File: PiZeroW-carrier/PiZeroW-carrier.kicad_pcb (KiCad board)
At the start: 2 copper layers, 65 x 30 mm, 35 parts, among them CON1 BARREL_JACK, J1 PI40HAT, P1 USB_OTG, SW1 SW_PUSH, U1 BA50BC0WFP-E2CT, U2 BA06CC0WFP-E2CT

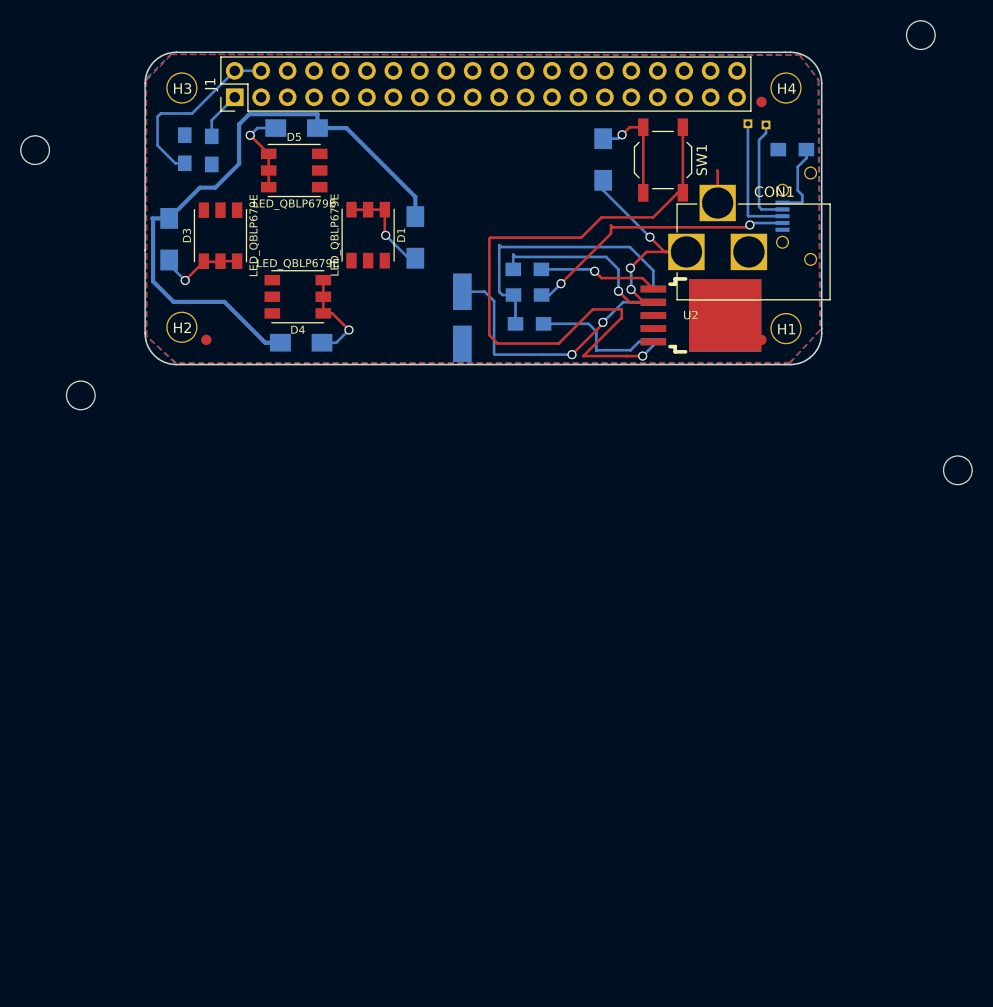
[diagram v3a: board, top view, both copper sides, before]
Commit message: cleanup some routes that the autorouter must have created
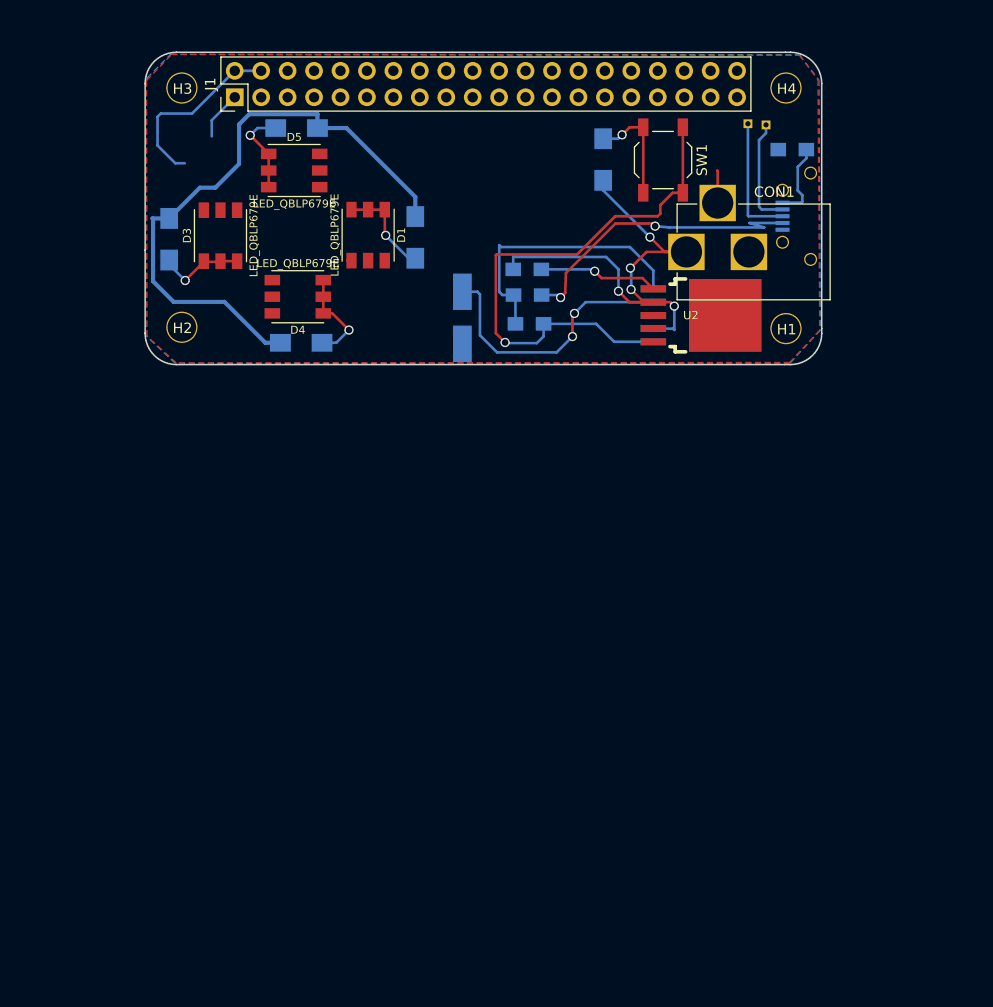
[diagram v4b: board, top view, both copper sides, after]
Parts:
- removed 1PIN (x4): P***, 1pin
- removed FID1, FID2, FID3: FIDUCIAL, DiscoCap:FIDUCIAL
- removed R10, R9: DNP, Resistors_SMD:R_0805_HandSoldering
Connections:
- net Net-(R2-Pad1) renamed /Power/PiDisable
- D6 pad 1: /Power/+5V -> (no net)
- J1 pad 1: /raspberrypi-gpio-40pin/P3V3_HAT -> (no net)
- J1 pad 10: Net-(J1-Pad10) -> (no net)
- J1 pad 11: /raspberrypi-gpio-40pin/LEDEnable -> (no net)
- J1 pad 12: Net-(J1-Pad12) -> (no net)
- J1 pad 13: /raspberrypi-gpio-40pin/PiDisable -> (no net)
- J1 pad 15: Net-(J1-Pad15) -> (no net)
- J1 pad 16: Net-(J1-Pad16) -> (no net)
- J1 pad 17: Net-(J1-Pad17) -> (no net)
- J1 pad 18: Net-(J1-Pad18) -> (no net)
- J1 pad 19: Net-(J1-Pad19) -> (no net)
- J1 pad 21: Net-(J1-Pad21) -> (no net)
- J1 pad 22: Net-(J1-Pad22) -> (no net)
- J1 pad 23: Net-(J1-Pad23) -> (no net)
- J1 pad 24: Net-(J1-Pad24) -> (no net)
- J1 pad 26: Net-(J1-Pad26) -> (no net)
- J1 pad 27: /raspberrypi-gpio-40pin/SDA -> (no net)
- J1 pad 28: /raspberrypi-gpio-40pin/SCL -> (no net)
- J1 pad 29: Net-(J1-Pad29) -> (no net)
- J1 pad 3: Net-(J1-Pad3) -> (no net)
- J1 pad 31: Net-(J1-Pad31) -> (no net)
- J1 pad 32: Net-(J1-Pad32) -> (no net)
- J1 pad 33: Net-(J1-Pad33) -> (no net)
- J1 pad 35: Net-(J1-Pad35) -> (no net)
- J1 pad 36: Net-(J1-Pad36) -> (no net)
- J1 pad 37: Net-(J1-Pad37) -> (no net)
- J1 pad 38: Net-(J1-Pad38) -> (no net)
- J1 pad 40: Net-(J1-Pad40) -> (no net)
- J1 pad 5: Net-(J1-Pad5) -> (no net)
- J1 pad 7: Net-(J1-Pad7) -> (no net)
- J1 pad 8: Net-(J1-Pad8) -> (no net)
- R12 pad 1: +5V -> (no net)
- U2 pad 4: /Power/+6V -> (no net)
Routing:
- net /Power/PiDisable: track 77.0 -> 52.9 mm
- net +BATT: track 40.2 -> 46.7 mm, vias 4 -> 5
- net (no net): track 0.00 -> 5.18 mm
- net /raspberrypi-gpio-40pin/P3V3_HAT: track 4.67 -> 0.00 mm
- net Net-(P1-Pad4): track 26.6 -> 30.2 mm

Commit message: fix PiDisable/LEDEnable.  Need to connect them on the root sheet. Extra-duh
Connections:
- D1 pad 1: /Leds/GND -> GND
- D1 pad 2: /Leds/GND -> GND
- D1 pad 3: /Leds/GND -> GND
- D3 pad 1: /Leds/GND -> GND
- D3 pad 2: /Leds/GND -> GND
- D3 pad 3: /Leds/GND -> GND
- D4 pad 1: /Leds/GND -> GND
- D4 pad 2: /Leds/GND -> GND
- D4 pad 3: /Leds/GND -> GND
- D5 pad 1: /Leds/GND -> GND
- D5 pad 2: /Leds/GND -> GND
- D5 pad 3: /Leds/GND -> GND
- J1 pad 11: (no net) -> /Power/LEDEnable
- J1 pad 13: (no net) -> /Power/PiDisable

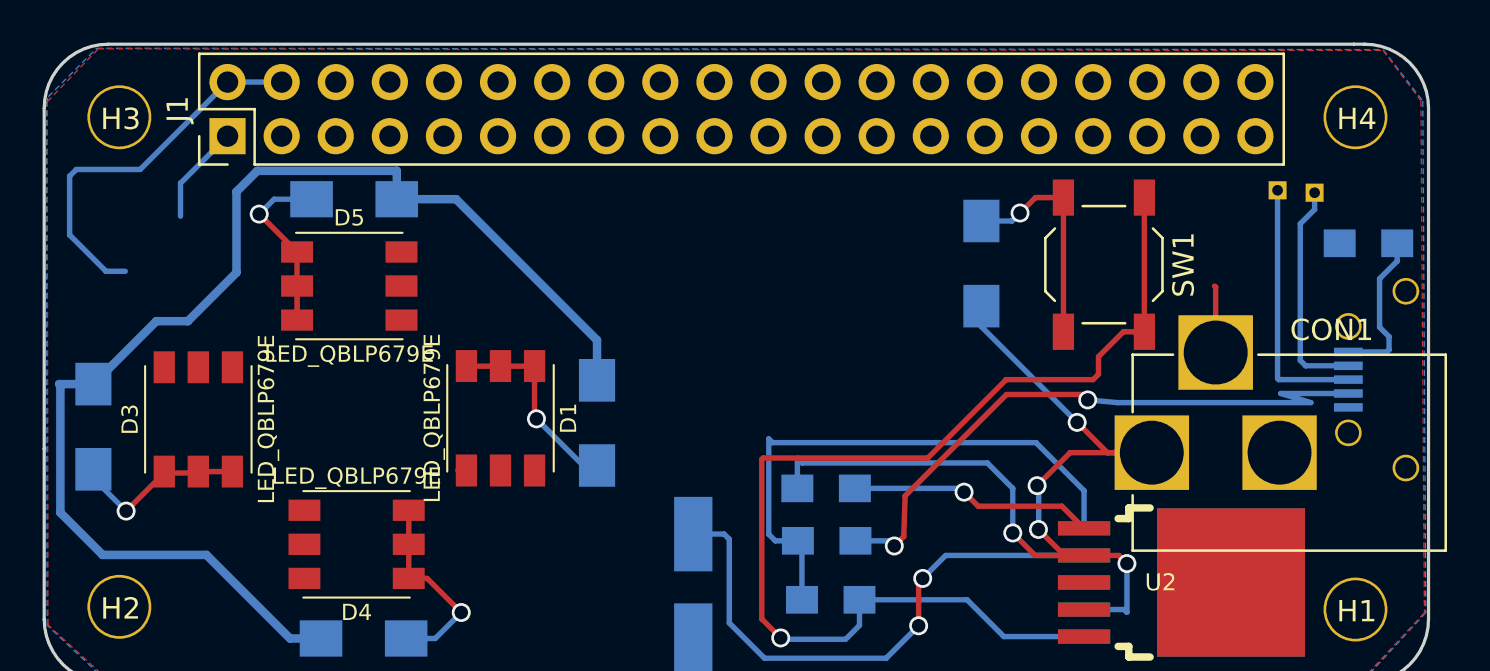
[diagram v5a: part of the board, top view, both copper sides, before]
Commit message: route LEDEnable and PiDisable. fix 40pin Gnds
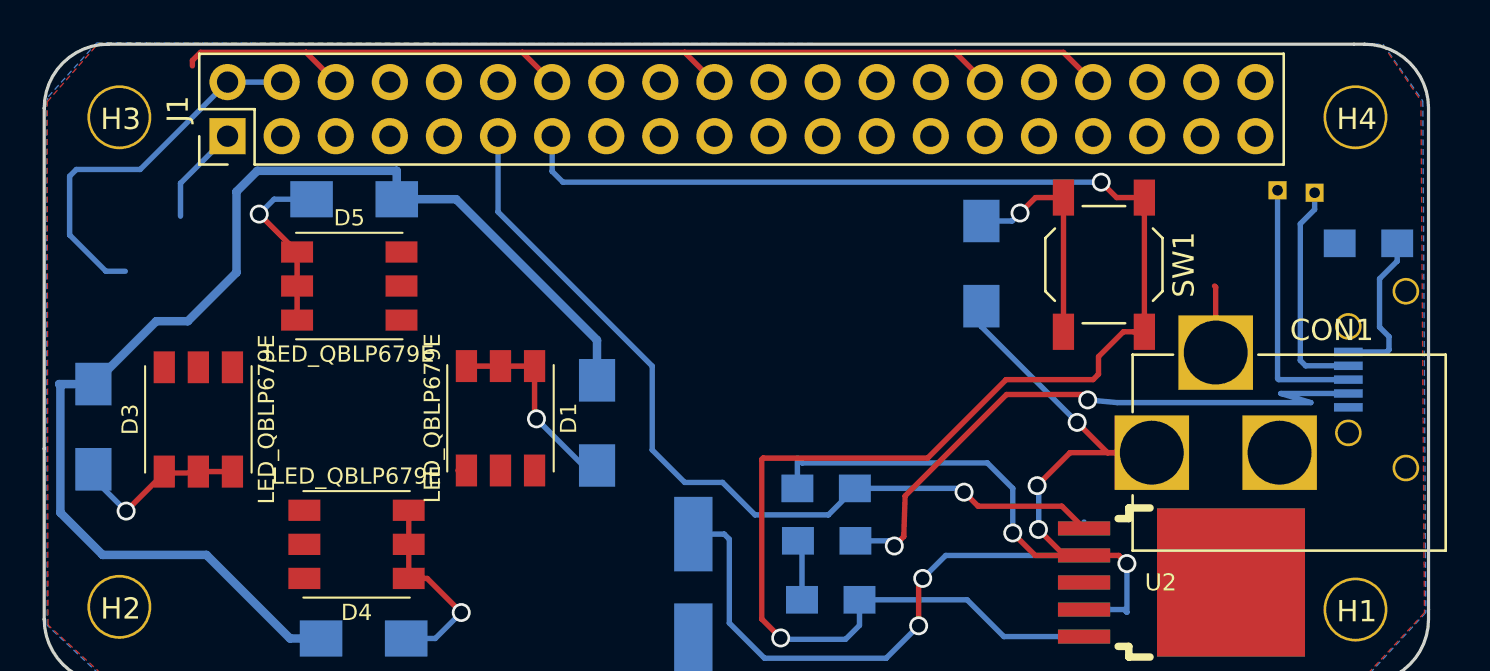
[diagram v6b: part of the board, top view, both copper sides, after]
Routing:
- net /Power/PiDisable: track 52.9 -> 82.9 mm, vias 1 -> 2
- net /Power/LEDEnable: track 11.5 -> 40.6 mm
- net GND: track 30.3 -> 57.9 mm
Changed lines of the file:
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@@
   (general
     (links 65)
-    (no_connects 20)
+    (no_connects 2)
     (area 109.424999 79.424999 174.575001 109.575001)
     (thickness 1.6)
     (drawings 12)
-    (tracks 172)
+    (tracks 191)
     (zones 0)
     (modules 26)
@@
   (segment (start 143.31188 81.71942) (end 143.31188 81.97342) (width 0.254) (layer F.Cu) (net 0))
   (segment (start 148.39188 81.71942) (end 148.39188 81.84642) (width 0.254) (layer B.Cu) (net 0))
+  (segment (start 152.273 79.883) (end 157.353 79.883) (width 0.254) (layer F.Cu) (net 1))
+  (segment (start 157.353 79.883) (end 158.75 81.28) (width 0.254) (layer F.Cu) (net 1) (status 800000))
+  (segment (start 139.573 79.883) (end 152.273 79.883) (width 0.254) (layer F.Cu) (net 1))
+  (segment (start 152.273 79.883) (end 153.67 81.28) (width 0.254) (layer F.Cu) (net 1) (status 800000))
+  (segment (start 131.953 79.883) (end 139.573 79.883) (width 0.254) (layer F.Cu) (net 1))
+  (segment (start 139.573 79.883) (end 140.97 81.28) (width 0.254) (layer F.Cu) (net 1) (status 800000))
+  (segment (start 121.793 79.883) (end 131.953 79.883) (width 0.254) (layer F.Cu) (net 1))
+  (segment (start 131.953 79.883) (end 133.35 81.28) (width 0.254) (layer F.Cu) (net 1) (status 800000))
+  (segment (start 116.459 80.518) (end 116.459 80.264) (width 0.254) (layer F.Cu) (net 1))
+  (segment (start 121.793 79.883) (end 123.19 81.28) (width 0.254) (layer F.Cu) (net 1) (status 800000))
+  (segment (start 116.84 79.883) (end 121.793 79.883) (width 0.254) (layer F.Cu) (net 1))
+  (segment (start 116.459 80.264) (end 116.84 79.883) (width 0.254) (layer F.Cu) (net 1))
   (segment (start 164.5059 93.979) (end 164.5059 90.9094) (width 0.254) (layer F.Cu) (net 1))
   (segment (start 164.5059 90.9094) (end 164.4523 90.8558) (width 0.254) (layer F.Cu) (net 1))
   (segment (start 158.325 102.235) (end 158.325 101.9361) (width 0.254) (layer B.Cu) (net 1))
-  (segment (start 144.8905 102.8192) (end 143.8275 102.8192) (width 0.254) (layer B.Cu) (net 1))
-  (segment (start 158.325 100.4638) (end 158.325 102.235) (width 0.254) (layer B.Cu) (net 1))
-  (segment (start 156.0703 98.2091) (end 158.325 100.4638) (width 0.254) (layer B.Cu) (net 1))
-  (segment (start 143.7005 98.2091) (end 156.0703 98.2091) (width 0.254) (layer B.Cu) (net 1))
-  (segment (start 143.5227 98.0313) (end 143.7005 98.2091) (width 0.254) (layer B.Cu) (net 1))
-  (segment (start 143.5227 102.5144) (end 143.5227 98.0313) (width 0.254) (layer B.Cu) (net 1))
-  (segment (start 143.8275 102.8192) (end 143.5227 102.5144) (width 0.254) (layer B.Cu) (net 1))
   (segment (start 145.081 105.5878) (end 145.081 103.0097) (width 0.254) (layer B.Cu) (net 1))
   (segment (start 145.081 103.0097) (end 144.8905 102.8192) (width 0.254) (layer B.Cu) (net 1))
@@
   (via (at 155.321 87.4268) (size 0.889) (drill 0.635) (layers F.Cu B.Cu) (net 13))
   (segment (start 156.0453 86.7025) (end 155.321 87.4268) (width 0.254) (layer F.Cu) (net 13))
+  (segment (start 130.81 83.82) (end 130.81 87.376) (width 0.254) (layer B.Cu) (net 14) (status 400000))
+  (segment (start 146.3205 101.6) (end 147.5651 100.3554) (width 0.254) (layer B.Cu) (net 14) (status 800000))
+  (segment (start 142.875 101.6) (end 146.3205 101.6) (width 0.254) (layer B.Cu) (net 14))
+  (segment (start 141.351 100.076) (end 142.875 101.6) (width 0.254) (layer B.Cu) (net 14))
+  (segment (start 139.573 100.076) (end 141.351 100.076) (width 0.254) (layer B.Cu) (net 14))
+  (segment (start 138.049 98.552) (end 139.573 100.076) (width 0.254) (layer B.Cu) (net 14))
+  (segment (start 138.049 94.615) (end 138.049 98.552) (width 0.254) (layer B.Cu) (net 14))
+  (segment (start 130.81 87.376) (end 138.049 94.615) (width 0.254) (layer B.Cu) (net 14))
   (segment (start 147.5651 100.3554) (end 152.5143 100.3554) (width 0.254) (layer B.Cu) (net 14))
   (segment (start 157.2836 101.1936) (end 158.325 102.235) (width 0.254) (layer F.Cu) (net 14))
@@
   (segment (start 128.8415 86.7791) (end 126.0536 86.7791) (width 0.4) (layer B.Cu) (net 15))
   (segment (start 135.4582 93.3958) (end 128.8415 86.7791) (width 0.4) (layer B.Cu) (net 15))
+  (segment (start 133.35 83.82) (end 133.35 85.471) (width 0.254) (layer B.Cu) (net 16) (status 400000))
+  (segment (start 159.8545 86.7025) (end 161.158 86.7025) (width 0.254) (layer F.Cu) (net 16) (status 800000))
+  (segment (start 159.131 85.979) (end 159.8545 86.7025) (width 0.254) (layer F.Cu) (net 16))
+  (via (at 159.131 85.979) (size 0.889) (drill 0.635) (layers F.Cu B.Cu) (net 16))
+  (segment (start 133.858 85.979) (end 159.131 85.979) (width 0.254) (layer B.Cu) (net 16))
+  (segment (start 133.35 85.471) (end 133.858 85.979) (width 0.254) (layer B.Cu) (net 16))
   (segment (start 161.158 93.0025) (end 160.172 93.0025) (width 0.254) (layer F.Cu) (net 16))
   (segment (start 147.781 106.7905) (end 147.781 105.5878) (width 0.254) (layer B.Cu) (net 16))
@@
     (polygon
       (pts
-        (xy 172.3644 79.7941) (xy 174.1424 82.1563) (xy 174.3075 106.1974) (xy 171.4246 109.2962) (xy 112.4966 109.347)
-        (xy 109.6772 106.7689) (xy 109.6391 82.2071) (xy 112.0394 79.7179)
+        (xy 172.3644 79.5401) (xy 174.1424 82.1563) (xy 174.3075 106.1974) (xy 171.4246 109.2962) (xy 112.4966 109.347)
+        (xy 109.6772 106.7689) (xy 109.6391 82.2071) (xy 112.0394 79.4639)
       )
     )
@@
     (polygon
       (pts
-        (xy 111.9632 79.6925) (xy 172.3644 79.756) (xy 174.2313 82.169) (xy 174.371 106.1847) (xy 171.45 109.3597)
+        (xy 111.9632 79.4385) (xy 172.3644 79.502) (xy 174.2313 82.169) (xy 174.371 106.1847) (xy 171.45 109.3597)
         (xy 112.395 109.3724) (xy 109.6391 106.7816) (xy 109.601 82.296) (xy 109.6899 81.9658)
       )

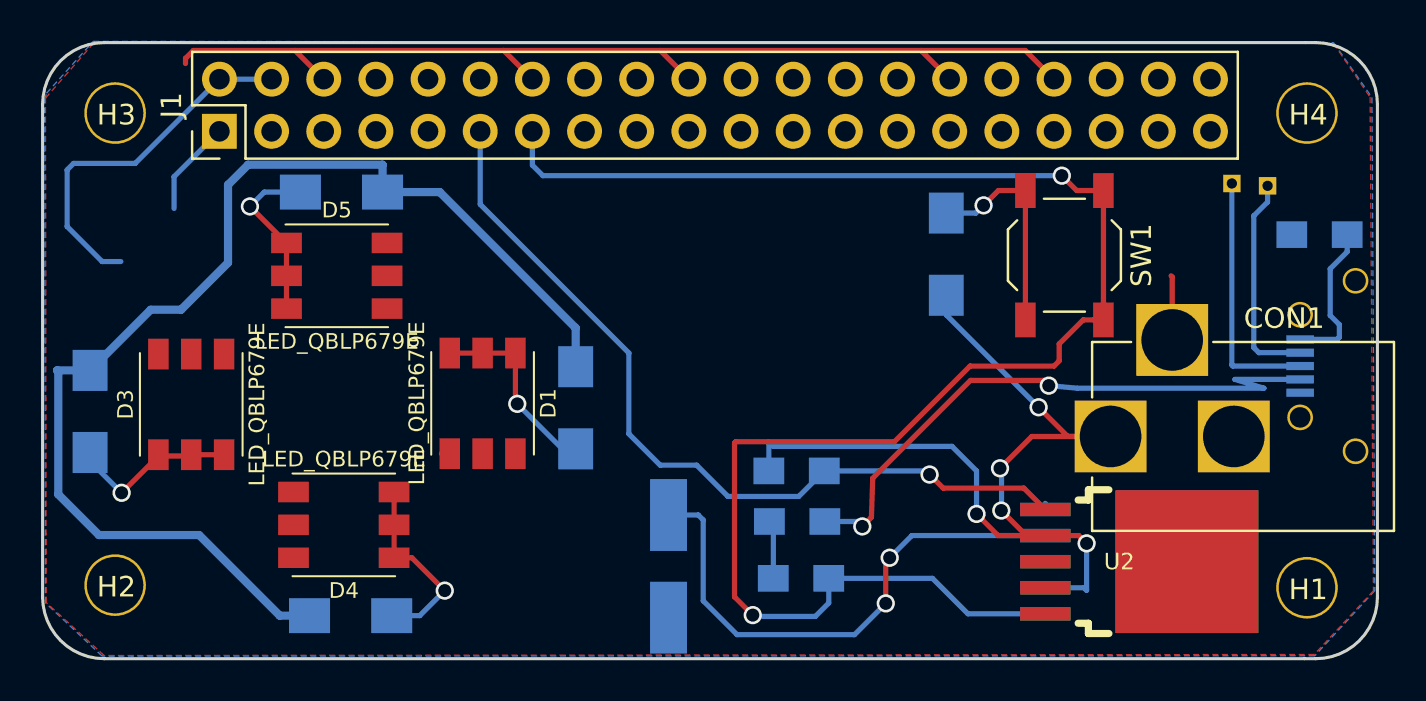
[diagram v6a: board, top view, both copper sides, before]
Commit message: tricky via placement to link a ground pour that became an island
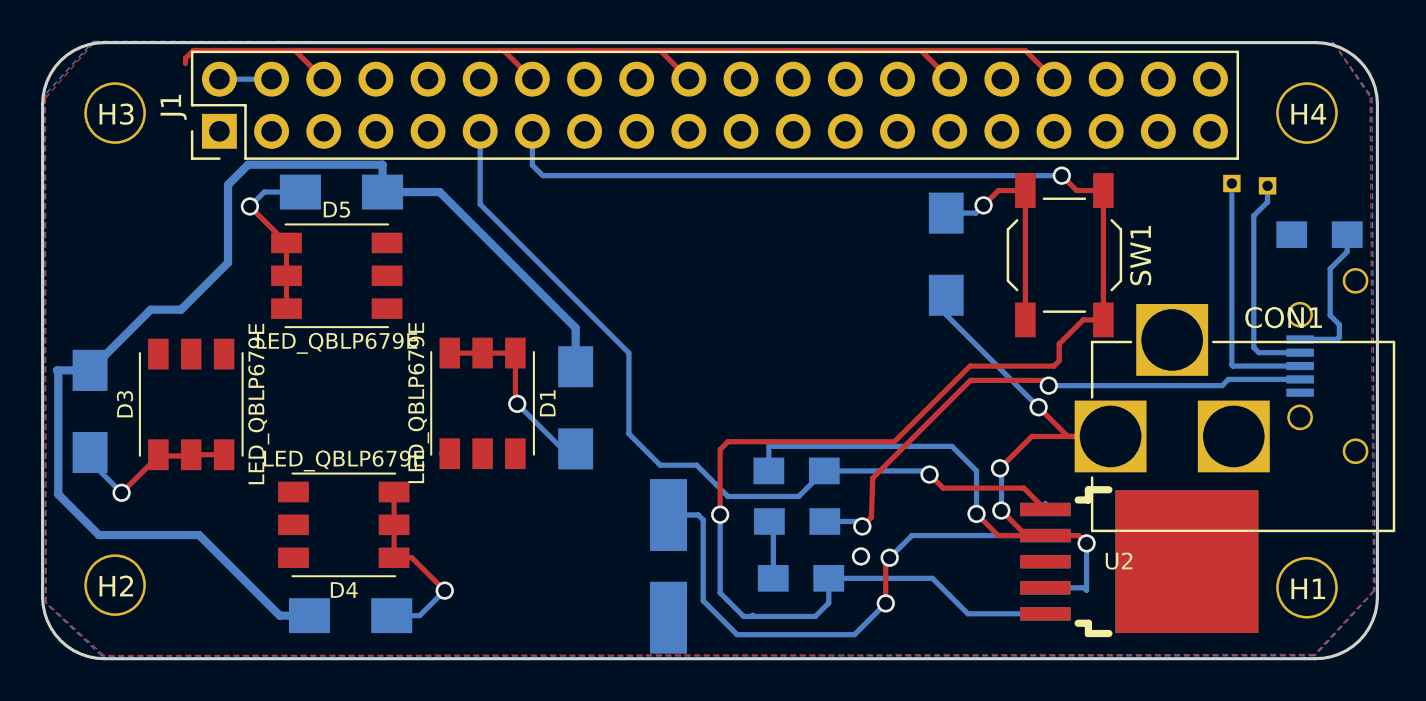
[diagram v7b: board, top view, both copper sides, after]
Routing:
- net /raspberrypi-gpio-40pin/P5V_HAT: track 18.0 -> 2.67 mm
- net (no net): track 5.18 -> 0.51 mm
- net GND: track 57.9 -> 54.7 mm, vias 0 -> 1
- net Net-(P1-Pad4): track 30.2 -> 27.5 mm
- net /Power/PiDisable: track 82.9 -> 84.1 mm
